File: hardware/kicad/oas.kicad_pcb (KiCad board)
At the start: 2 copper layers, 120 x 103.5 mm, 69 parts, among them J1 Phoenix_MSTBA_2,5/3-G-5,08 (2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, J10 Native-USB recovery (DNP), J2 UART/Boot Recovery (DNP), J3 JST SM06B-GHS-TB (SEN66 conne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, J4 1x5 P1.27mm header (HLK-LD241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, J5 ESP32 row A (pins 1..15, ante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, J6 ESP32 row B (pins 16..30, USB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, J7 MIKROE mikroBUS pins 1..8 (AN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, J8 MIKROE mikroBUS pins 9..16 (P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, J9 JST SM04B-SRSS-TB (Qwiic / St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, Q1 AO3401A, SW1 C&K PTS645VK392LFS, U1 LM2596S-5.0, U2 TPS62933

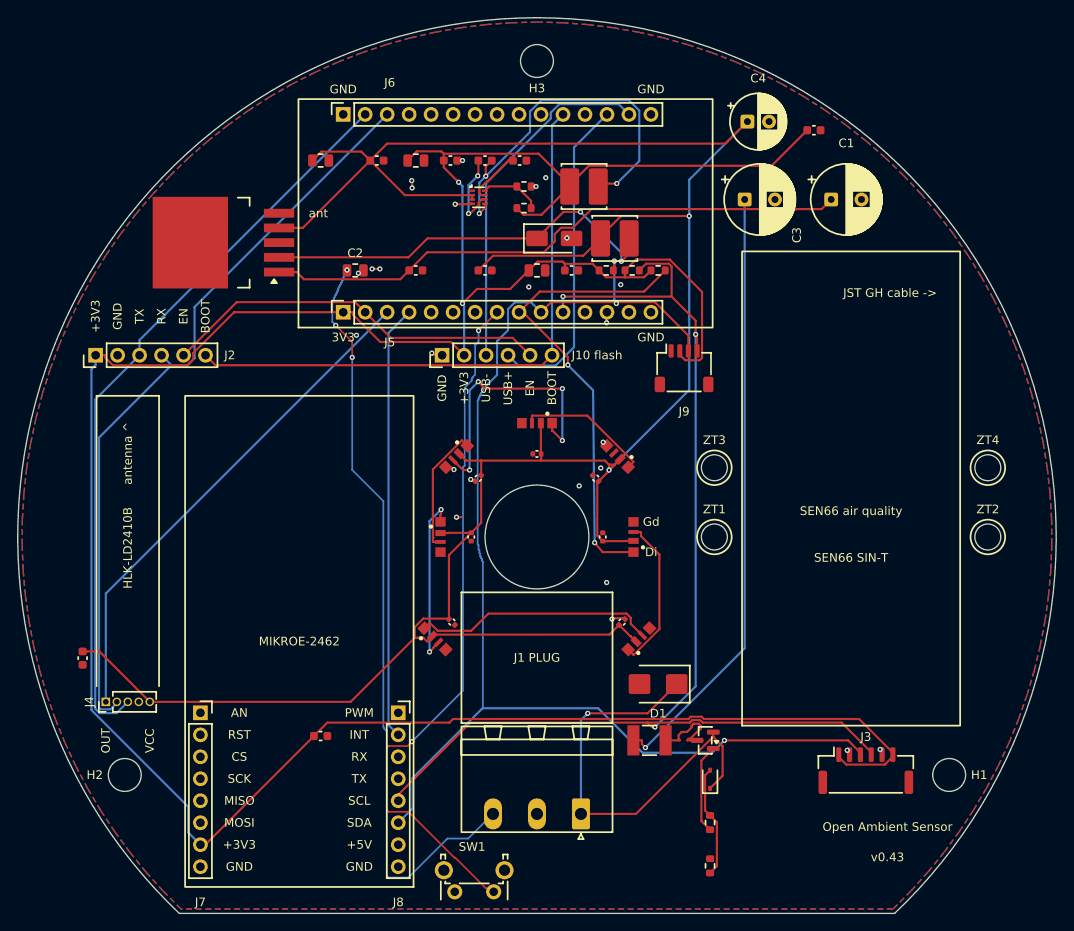
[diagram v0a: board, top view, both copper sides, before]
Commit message: Revert "feat(routing): v0.50 full routing rework — Freerouting + grid-A* + GND stitch"
This reverts commit dd98a8b5e2c532be2b86d95f3e04231419d46720.
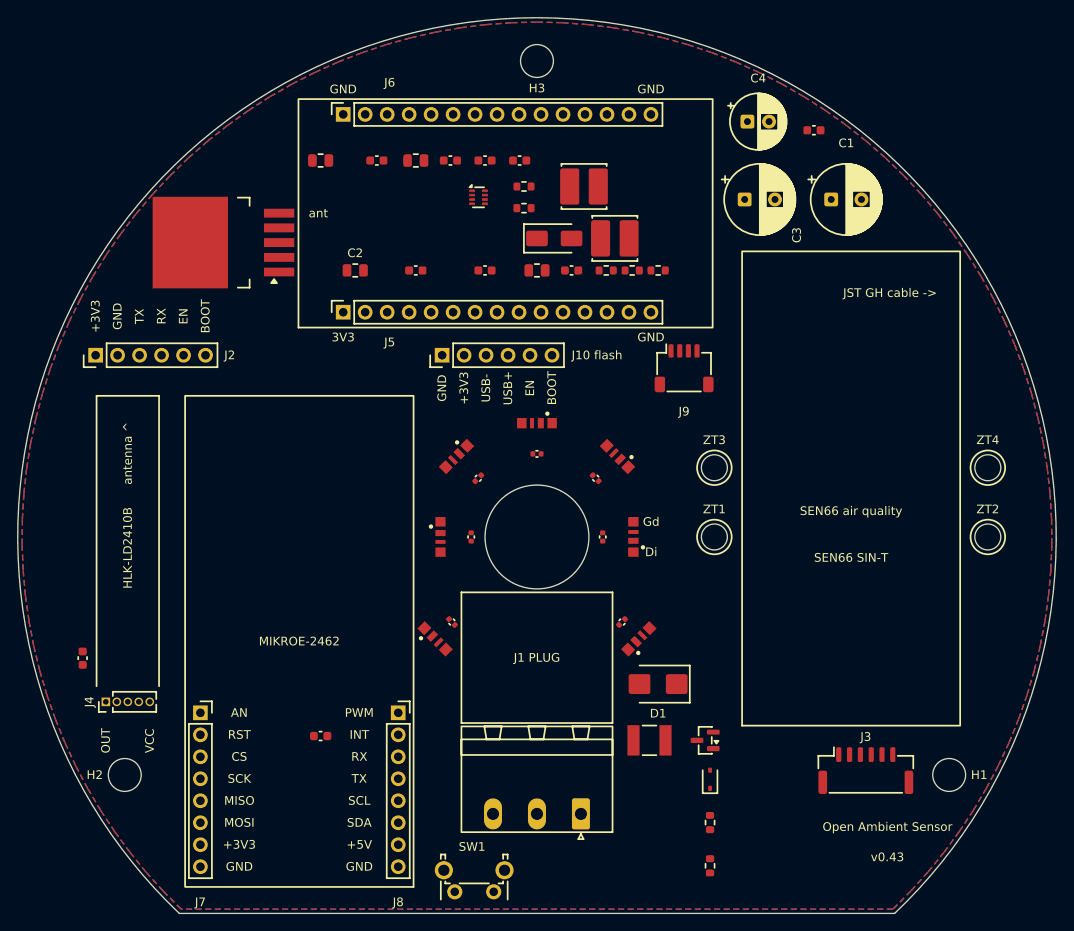
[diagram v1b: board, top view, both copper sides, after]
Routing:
- net +3V3: track 337.5 -> 0.00 mm, vias 2 -> 0
- net +5V: track 292.7 -> 0.00 mm, vias 2 -> 0
- net /IO/I2C_SDA: track 144.2 -> 0.00 mm, vias 3 -> 0
- net +24V: track 139.7 -> 0.00 mm, vias 1 -> 0
- net /IO/I2C_SCL: track 138.7 -> 0.00 mm, vias 3 -> 0
- net Earth_Protective: track 88.9 -> 0.00 mm, vias 3 -> 0
- net /MCU/UART_RX: track 87.6 -> 0.00 mm
- net /MCU/UART_TX: track 86.1 -> 0.00 mm
- net /IO/BTN: track 80.4 -> 0.00 mm, vias 2 -> 0
- net /IO/BOOT: track 69.4 -> 0.00 mm
- net /MCU/LD2410_OUT: track 58.5 -> 0.00 mm
- net /MCU/WS2812_DIN: track 54.3 -> 0.00 mm, vias 2 -> 0
- net /MCU/NFC_FD: track 50.3 -> 0.00 mm
- net Net-(D1-K): track 50.2 -> 0.00 mm, vias 1 -> 0
- net Net-(D2-K): track 47.7 -> 0.00 mm, vias 2 -> 0
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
